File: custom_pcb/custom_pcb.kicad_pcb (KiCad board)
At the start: 2 copper layers, 285 x 152 mm, 311 parts, among them J1 USB_mini_micro_B, K0 KEYSW, K1 KEYSW, K10 KEYSW, K11 KEYSW, K12 KEYSW, K13 KEYSW, K14 KEYSW, K15 KEYSW, K16 KEYSW, K17 KEYSW, K18 KEYSW, K19 KEYSW, K2 KEYSW, K20 KEYSW, K21 KEYSW, K22 KEYSW, K23 KEYSW, K24 KEYSW, K25 KEYSW, K26 KEYSW, K27 KEYSW, K28 KEYSW, K29 KEYSW, K3 KEYSW, K30 KEYSW, K31 KEYSW, K32 KEYSW, K33 KEYSW, K34 KEYSW, K35 KEYSW, K36 KEYSW, K37 KEYSW, K38 KEYSW, K39 KEYSW, K4 KEYSW, K40 KEYSW, K41 KEYSW, K42 KEYSW, K43 KEYSW, K44 KEYSW, K45 KEYSW, K46 KEYSW, K47 KEYSW, K48 KEYSW, K49 KEYSW, K5 KEYSW, K50 KEYSW, K51 KEYSW, K52 KEYSW, K53 KEYSW, K54 KEYSW, K55 KEYSW, K56 KEYSW, K57 KEYSW, K58 KEYSW, K59 KEYSW, K6 KEYSW, K60 KEYSW, K63 KEYSW, K64 KEYSW, K65 KEYSW, K66 KEYSW, K67 KEYSW, K68 KEYSW, K69 KEYSW, K7 KEYSW, K70 KEYSW, K71 KEYSW, K72 KEYSW, K73 KEYSW, K74 KEYSW, K75 KEYSW, K76 KEYSW, K77 KEYSW, K78 KEYSW, K79 KEYSW, K8 KEYSW, K80 KEYSW, K81 KEYSW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

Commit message: more routing
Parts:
- added V5: CONN_01X01, cherry_rgb:VIA127, F.Cu at (122.6, 43.4)
- moved RSW0 2.17 mm to (100.2, 30.2)
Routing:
- net +5V: track 90.3 -> 180.9 mm, vias 0 -> 4
- net +3V3: track 259.6 -> 255.7 mm

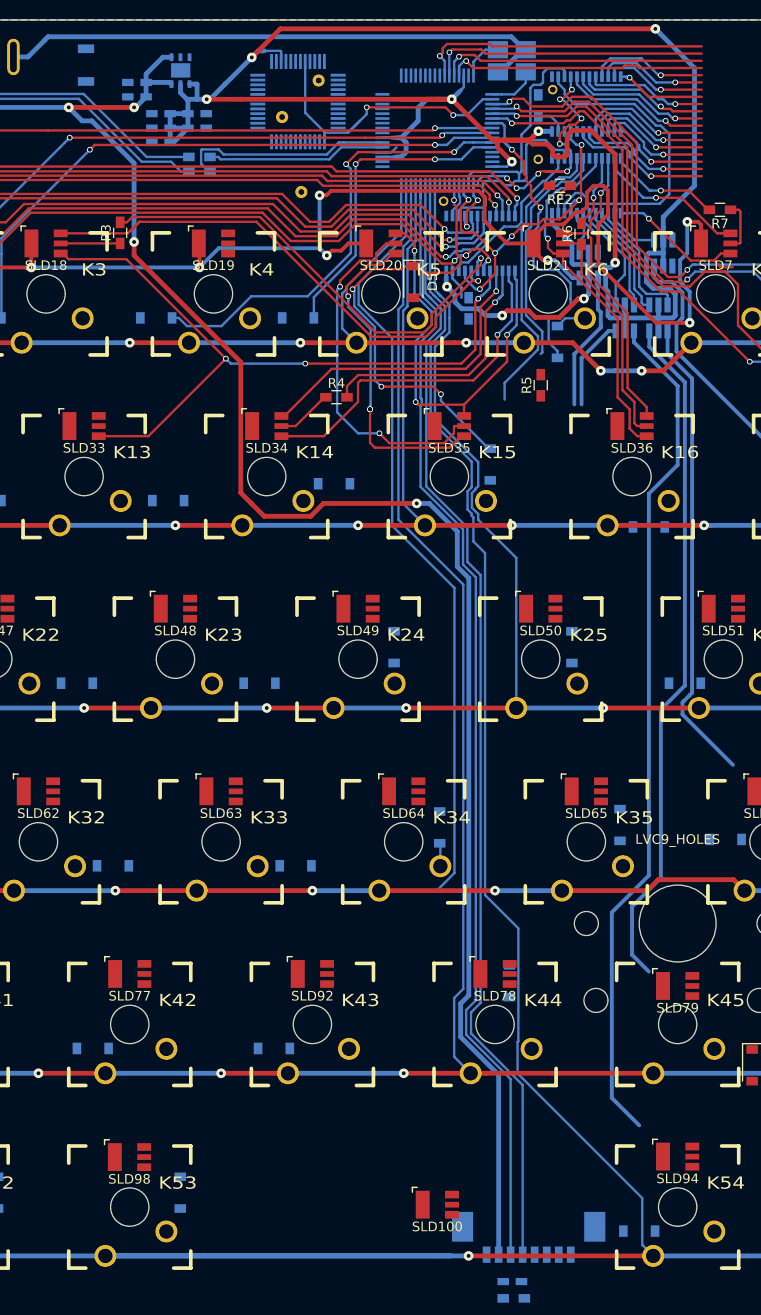
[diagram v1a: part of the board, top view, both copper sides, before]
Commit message: push routing mode is dangerous, it can move tracks into positions that cause infinite looping in freerouter because they block all ways to access a pad
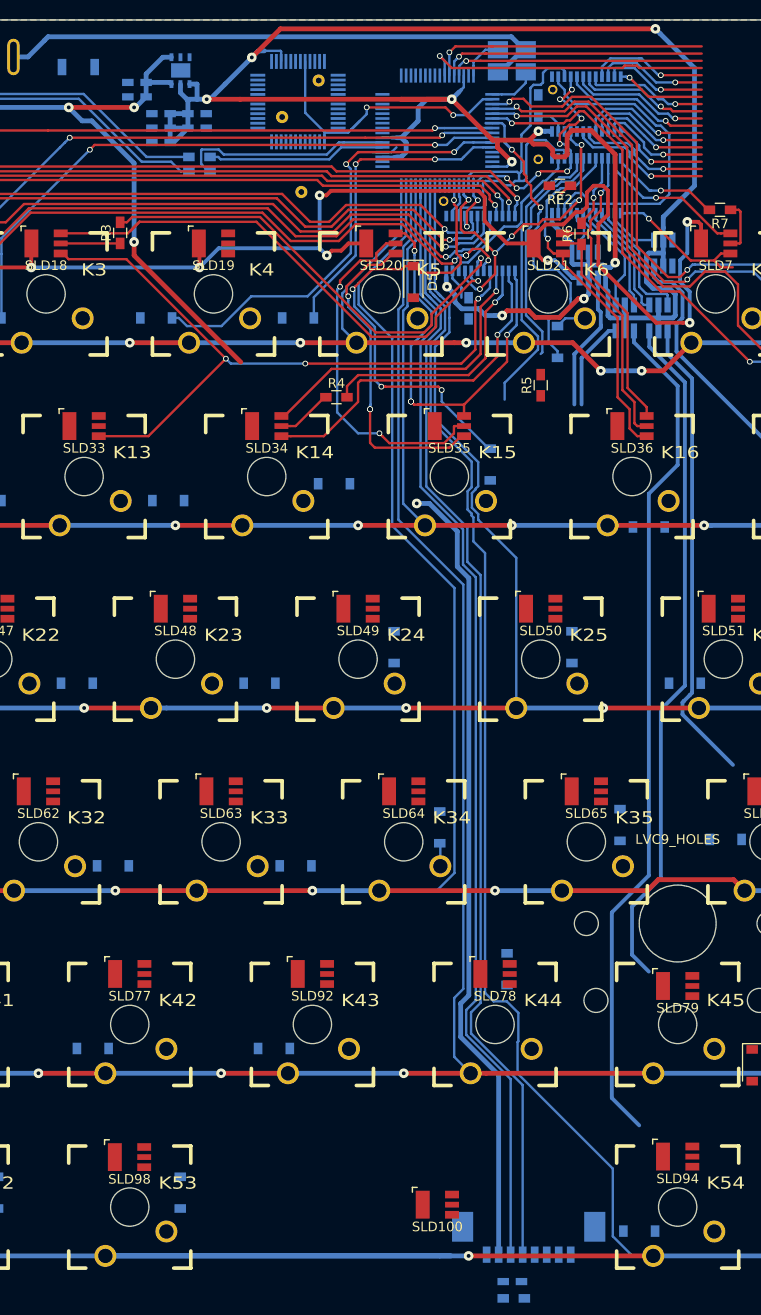
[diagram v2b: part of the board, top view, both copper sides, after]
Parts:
- moved D44 1.27 mm to (144.0, 124.2)
- moved RSW0 0.82 mm to (99.4, 30.4), turned to 0 degrees
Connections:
- U1 pad 26: c14 -> c11
- U1 pad 27: c13 -> c14
- U1 pad 28: c12 -> c13
- U1 pad 29: c11 -> c12
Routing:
- net +5V: track 180.9 -> 147.5 mm
- net LED_LE: track 38.9 -> 33.0 mm
- net +3V3: track 255.7 -> 252.3 mm
- net c11: track 27.0 -> 30.2 mm
- net r5: track 443.9 -> 446.0 mm
- net c14: track 30.4 -> 29.0 mm
- net c13: track 29.0 -> 27.6 mm
- net c12: track 27.7 -> 26.5 mm
- net blue5: track 43.4 -> 44.3 mm, vias 3 -> 4

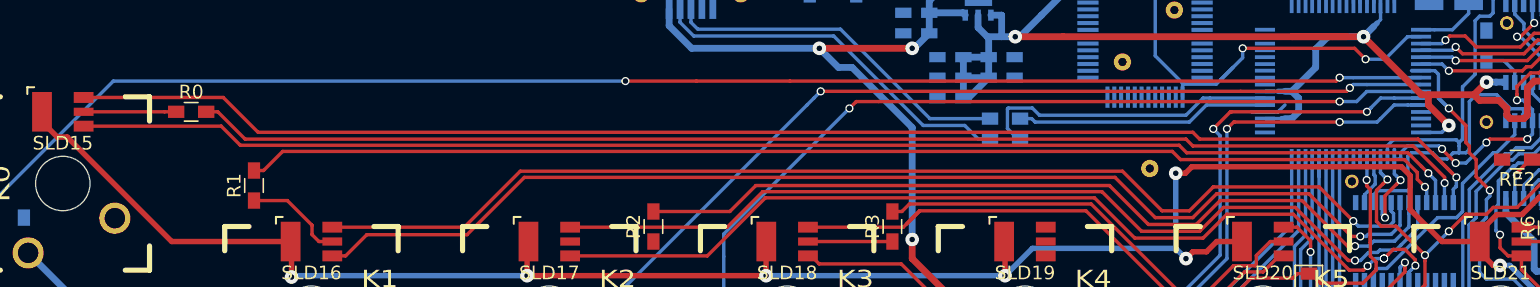
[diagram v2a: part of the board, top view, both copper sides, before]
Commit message: seems that there was a connected/disconnected track that was causing bugs
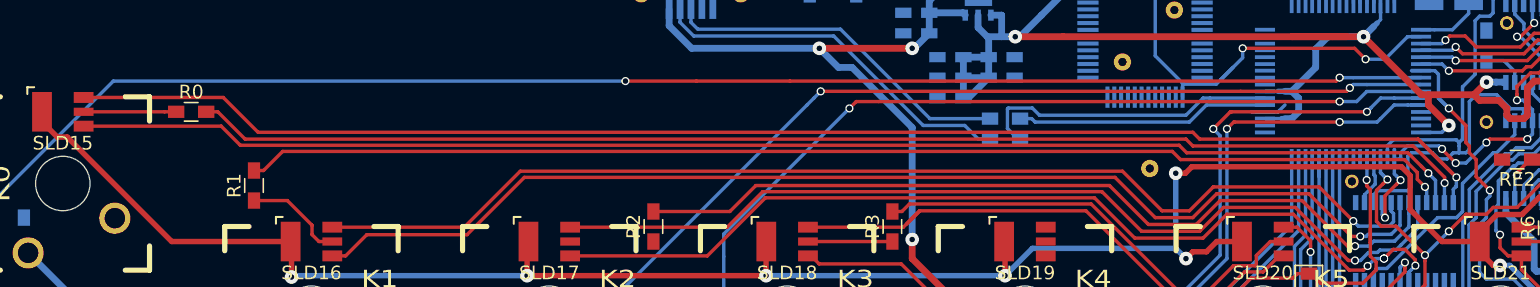
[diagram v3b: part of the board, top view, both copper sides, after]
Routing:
- net blue0: track 107.1 -> 111.0 mm
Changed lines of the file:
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@@
     (thickness 1.6)
     (drawings 6)
-    (tracks 1750)
+    (tracks 1751)
     (zones 0)
     (modules 312)
@@
   (segment (start 44.525 40.3) (end 54.600042 40.3) (width 0.25) (layer F.Cu) (net 126))
   (segment (start 54.600042 40.3) (end 56 41.699958) (width 0.25) (layer F.Cu) (net 126))
-  (segment (start 142.25 41.25) (end 143.25 42.25) (width 0.25) (layer F.Cu) (net 127))
-  (segment (start 57.3 40.75) (end 125.75 40.75) (width 0.25) (layer F.Cu) (net 127))
+  (segment (start 144.825 45.9) (end 144.825 44.925) (width 0.25) (layer B.Cu) (net 127))
+  (segment (start 145.049999 44.049999) (end 145.049999 44.700001) (width 0.25) (layer B.Cu) (net 127))
+  (segment (start 145.049999 44.700001) (end 144.825 44.925) (width 0.25) (layer B.Cu) (net 127))
   (segment (start 142.25 41.25) (end 126.25 41.25) (width 0.25) (layer F.Cu) (net 127))
+  (segment (start 125.75 40.75) (end 57.3 40.75) (width 0.25) (layer F.Cu) (net 127))
   (segment (start 126.25 41.25) (end 125.75 40.75) (width 0.25) (layer F.Cu) (net 127))
-  (segment (start 44.525 38.2) (end 54.75 38.2) (width 0.25) (layer F.Cu) (net 127))
-  (segment (start 54.75 38.2) (end 57.3 40.75) (width 0.25) (layer F.Cu) (net 127))
+  (segment (start 57.3 40.75) (end 54.75 38.2) (width 0.25) (layer F.Cu) (net 127))
+  (segment (start 54.75 38.2) (end 44.525 38.2) (width 0.25) (layer F.Cu) (net 127))
+  (segment (start 145.049999 44.049999) (end 142.25 41.25) (width 0.25) (layer F.Cu) (net 127))
+  (segment (start 142.25 41.25) (end 143.25 42.25) (width 0.25) (layer F.Cu) (net 127))
   (segment (start 145.049999 44.049999) (end 143.25 42.25) (width 0.25) (layer F.Cu) (net 127))
   (via (at 145.049999 44.049999) (size 0.6) (drill 0.4) (layers F.Cu B.Cu) (net 127))
   (segment (start 143.25 42.25) (end 144.75 43.75) (width 0.25) (layer F.Cu) (net 127))
-  (segment (start 144.825 45.9) (end 144.825 44.925) (width 0.25) (layer B.Cu) (net 127))
-  (segment (start 144.825 44.925) (end 145.049999 44.700001) (width 0.25) (layer B.Cu) (net 127))
   (segment (start 145.049999 44.700001) (end 145 44.75) (width 0.25) (layer B.Cu) (net 127))
-  (segment (start 145.049999 44.049999) (end 145.049999 44.700001) (width 0.25) (layer B.Cu) (net 127))
   (segment (start 151 60.25) (end 151 65.5) (width 0.4) (layer B.Cu) (net 128))
   (segment (start 153.75 57.5) (end 151 60.25) (width 0.4) (layer B.Cu) (net 128))

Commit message: fixed crystal ground plane to match https://www.pjrc.com/store/ic_mkl02.html and https://forum.pjrc.com/threads/27397-Teensy-gt-Production?p=60903&viewfull=1#post60903
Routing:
- net GND: track 62.4 -> 65.1 mm
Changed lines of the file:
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@@
     (thickness 1.6)
     (drawings 6)
-    (tracks 1751)
+    (tracks 1756)
     (zones 0)
     (modules 312)
@@
   (segment (start 137.06 111.21) (end 137 111.15) (width 0.25) (layer B.Cu) (net 35))
   (segment (start 287.5 131.715) (end 286.675 132.54) (width 0.25) (layer B.Cu) (net 82))
+  (segment (start 140.75 32.5) (end 140 32.5) (width 0.25) (layer B.Cu) (net 89))
+  (segment (start 140.75 32.346601) (end 140.75 32.5) (width 0.25) (layer B.Cu) (net 89))
+  (segment (start 140.0012 31.285) (end 140.0012 32.25) (width 0.25) (layer B.Cu) (net 89))
+  (segment (start 140.75 32.346601) (end 140.097801 32.346601) (width 0.25) (layer B.Cu) (net 89))
+  (segment (start 140.097801 32.346601) (end 140.0012 32.25) (width 0.25) (layer B.Cu) (net 89))
   (segment (start 145.95 28.6) (end 145.8 28.6) (width 0.5) (layer B.Cu) (net 89))
   (segment (start 145.8 28.6) (end 144.449999 27.249999) (width 0.5) (layer B.Cu) (net 89))
@@
       (pts
         (xy 96.5 27.75) (xy 94.5 29.75) (xy 93 29.75) (xy 96 26.75) (xy 144.75 26.75)
-        (xy 145.25 27.25) (xy 147.5 27.25) (xy 147.5 32.25) (xy 141.5 32.25) (xy 141.5 27.75)
+        (xy 145.25 27.25) (xy 147.5 27.25) (xy 147.5 32.25) (xy 144.5 29.75) (xy 142 27.75)
+      )
+    )
+  )
+  (zone (net 0) (net_name "") (layer B.Cu) (hatch edge 0.508)
+    (connect_pads (clearance 0.25))
+    (min_thickness 0.254)
+    (keepout (tracks allowed) (vias allowed) (copperpour not_allowed))
+    (fill yes (arc_segments 16) (thermal_gap 0.508) (thermal_bridge_width 0.508))
+    (polygon
+      (pts
+        (xy 141.75 33.5) (xy 139.75 33.5) (xy 139.75 32.25) (xy 139.5 32.25) (xy 139 33.5)
+        (xy 139 33.75) (xy 141.75 33.75)
       )
     )

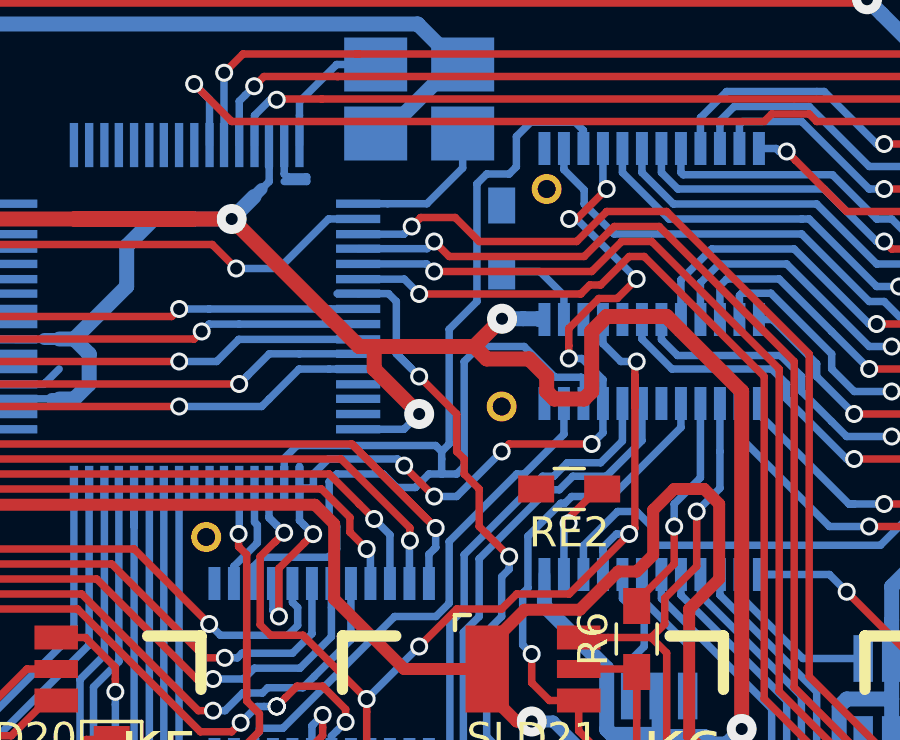
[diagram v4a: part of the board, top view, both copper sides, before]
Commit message: clock signal traces to same length
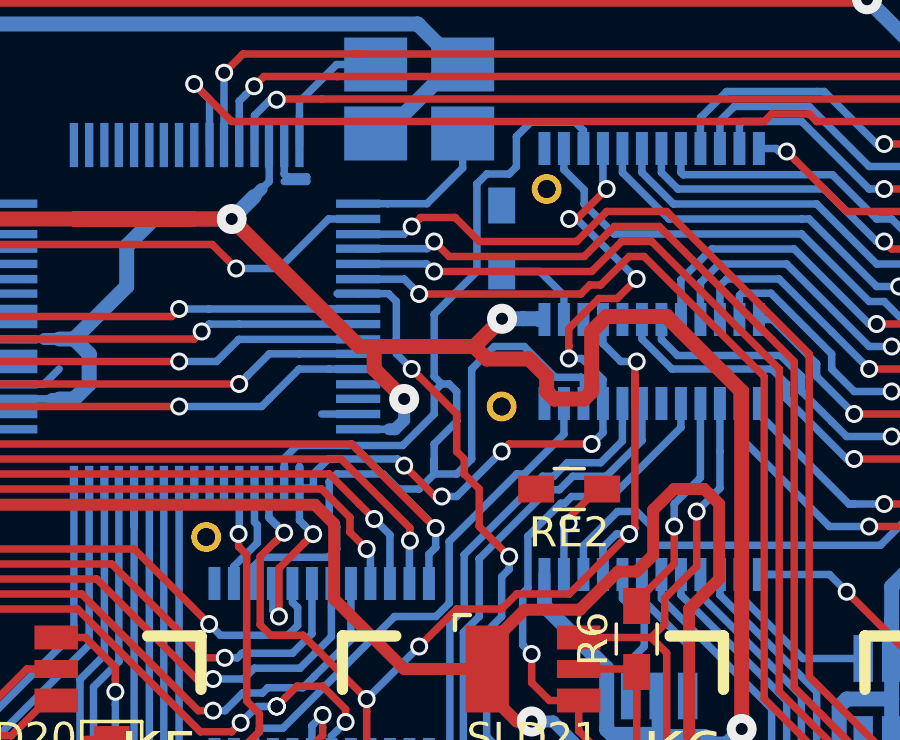
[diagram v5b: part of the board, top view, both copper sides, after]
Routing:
- net LED_CLK: track 42.3 -> 44.6 mm
- net GND: track 65.1 -> 66.3 mm
- net c6: track 33.3 -> 32.6 mm
- net +3V3: track 252.3 -> 251.7 mm

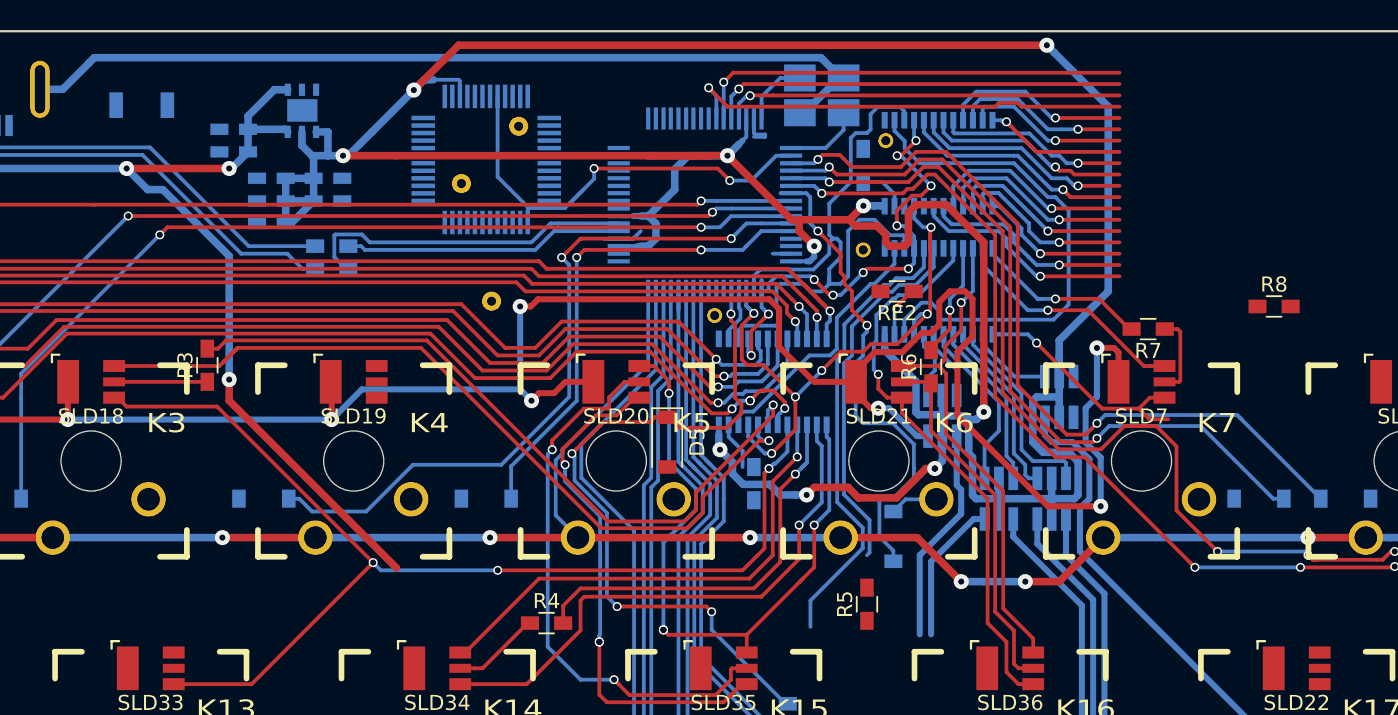
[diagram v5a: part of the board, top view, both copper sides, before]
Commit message: major rerouting to avoid any signals near the crystal and to get the rext resistors away from the led drivers
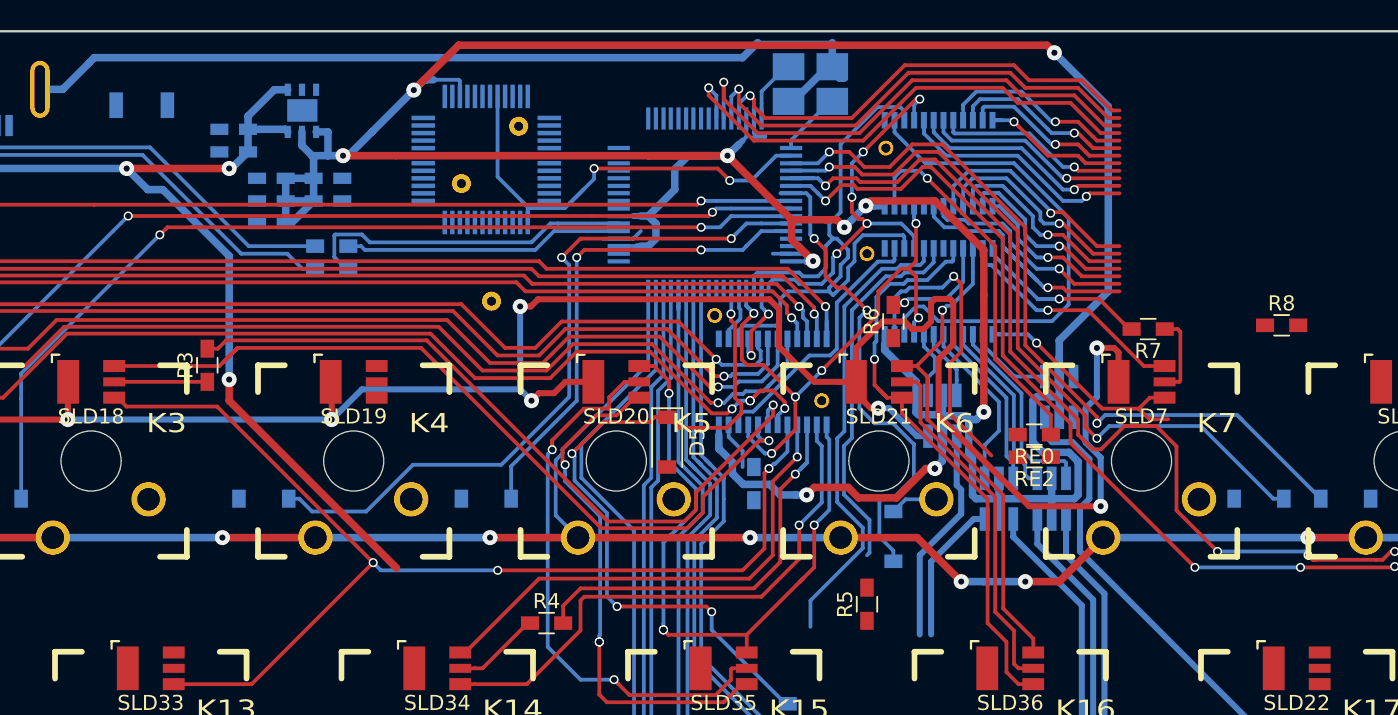
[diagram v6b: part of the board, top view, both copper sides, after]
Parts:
- added V6: CONN_01X01, cherry_rgb:VIA100, F.Cu at (144.5, 50.0)
- RE0: moved to F.Cu
- moved RE0 21.2 mm to (158.6, 52.2), turned to 180 degrees
- moved RE2 14.3 mm to (158.6, 53.8)
- moved R6 3.91 mm to (149.2, 44.8)
- moved R8 1.35 mm to (175.0, 45.0)
- moved Y0 1.06 mm to (143.8, 29.0)
- moved V1 0.50 mm to (148.8, 33.2)
- moved V0 0.35 mm to (147.5, 40.2)
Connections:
- U1 pad 27: c14 -> c12
- U1 pad 29: c12 -> c14
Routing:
- net Net-(LC0-Pad23): track 3.21 -> 24.9 mm, vias 0 -> 1
- net Net-(LC2-Pad23): track 3.47 -> 20.9 mm
- net c12: track 26.5 -> 33.4 mm
- net blue0: track 111.0 -> 105.9 mm
- net c13: track 27.6 -> 31.7 mm
- net green8: track 14.9 -> 18.7 mm
- net c11: track 30.2 -> 33.9 mm
- net +3V3: track 251.7 -> 249.3 mm
- net anode0: track 189.1 -> 191.4 mm
- net LED_CLK: track 44.6 -> 42.8 mm
- net c8: track 53.4 -> 51.9 mm
- net green6: track 37.5 -> 39.0 mm
- net Net-(LC0-Pad15): track 12.2 -> 13.5 mm
- net green10: track 13.8 -> 15.1 mm
- net blue9: track 13.0 -> 14.2 mm
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
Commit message: optimization around led drivers
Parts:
- moved RE1 14.8 mm to (146.0, 69.0)
- moved RE0 12.5 mm to (166.2, 62.1), turned to 270 degrees
- moved R12 1.55 mm to (256.1, 33.2)
- moved V0 0.43 mm to (147.8, 39.9)
- moved R6 0.25 mm to (149.2, 45.0)
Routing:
- net blue12: track 13.1 -> 143.0 mm
- net +3V3: track 249.3 -> 257.1 mm, vias 11 -> 10
- net c6: track 32.3 -> 36.7 mm
- net red6: track 23.7 -> 27.7 mm
- net (no net): track 0.00 -> 3.62 mm, vias 0 -> 1
- net Net-(LC2-Pad9): track 7.48 -> 9.40 mm
- net LED_CLK: track 42.8 -> 44.3 mm
- net Net-(LC0-Pad23): track 24.9 -> 23.6 mm
- net c8: track 51.9 -> 52.7 mm
- net LED_LE: track 34.0 -> 33.3 mm, vias 7 -> 6

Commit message: more close in optimization
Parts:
- D5: moved to B.Cu
- moved D5 7.32 mm to (133.2, 60.0), turned to 90 degrees
- moved V5 2.68 mm to (124.8, 45.0)
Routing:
- net c5: track 48.5 -> 33.6 mm, vias 4 -> 3
- net blue5: track 44.3 -> 58.4 mm, vias 4 -> 3
- net Net-(D5-Pad2): track 0.00 -> 7.82 mm
- net +3V3: track 257.1 -> 249.5 mm, vias 10 -> 9
- net r4: track 375.4 -> 379.5 mm
- net r1: track 325.8 -> 329.9 mm
- net green5: track 65.4 -> 68.9 mm, vias 3 -> 2
- net red5: track 37.3 -> 40.5 mm
- net anode0: track 191.0 -> 193.4 mm
- net c3: track 47.8 -> 45.5 mm
- net Net-(LC1-Pad19): track 48.5 -> 50.3 mm
- net blue3: track 55.2 -> 56.7 mm
- net blue0: track 106.0 -> 107.1 mm
- net r3: track 381.0 -> 382.1 mm
- net Net-(LC1-Pad9): track 89.1 -> 89.8 mm
